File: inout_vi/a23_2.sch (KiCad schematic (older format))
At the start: 27 parts, among them U23029 74HC02, U23030 74HC27, U23031 74HC02, U23032 74HC04, U23034 74HC02, U23035 74HC02, U23036 74HC02, U23037 74HC02, U23038 74HC27, U23039 74HC02, U23040 74HC02, U23041 74HC02, U23042 74HC02, U23043 74HC02, U23044 74HC02, U23045 74HC02, U23046 74HC02, U23047 74HC27, U23048 74HC04, U23049 74HC02, U23050 74HC02, U23051 74HC02, U23052 74HC02, U23053 74HC02, U23054 74HC04, U23055 74HC02, U23056 74HC02

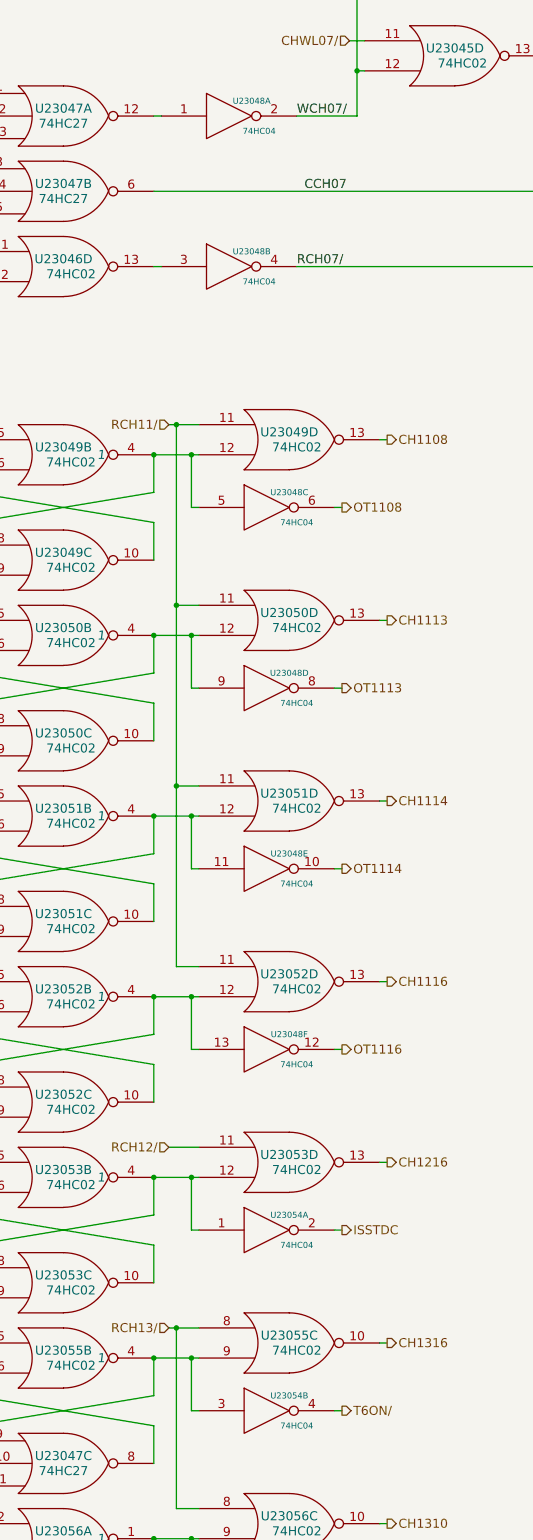
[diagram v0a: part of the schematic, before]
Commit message: Lots of initial conditions, some missed gates, and some wiring fixes
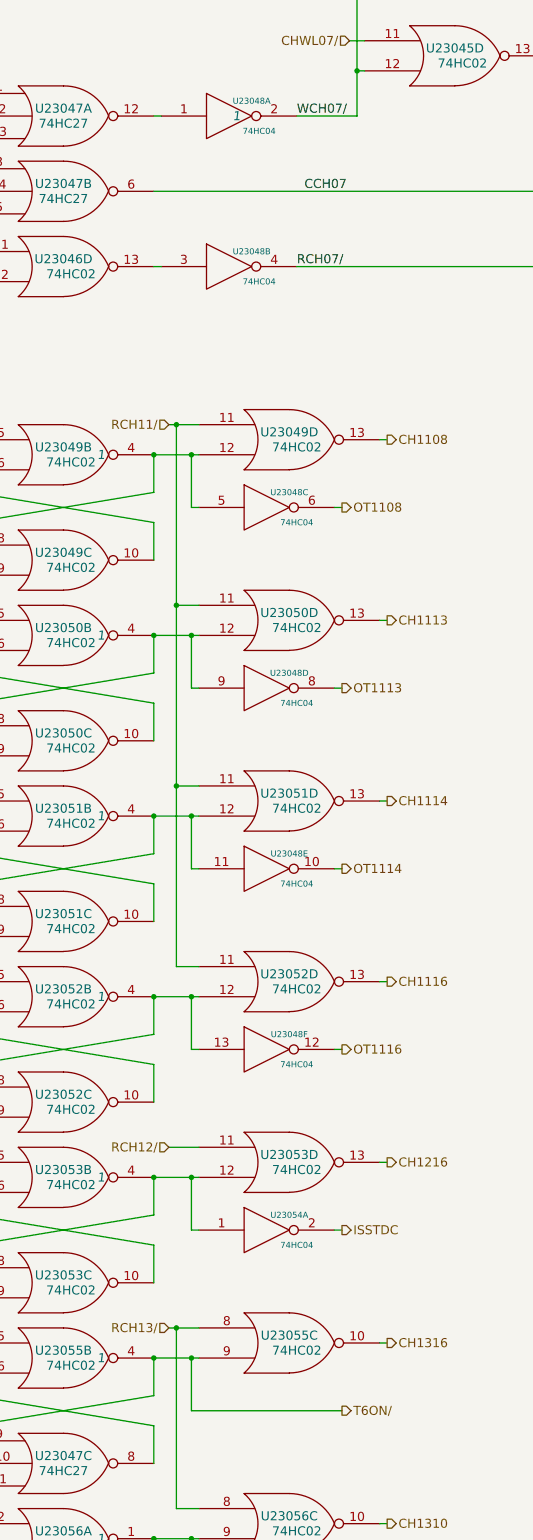
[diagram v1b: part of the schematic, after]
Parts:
- removed unit 2 of U23054
- U23048: Initial (none) -> 1
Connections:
- net T6ON/: now also U23047.9, U23055.4, U23055.9
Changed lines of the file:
@@
 F 2 "" H 13700 3850 60  0000 C CNN
 F 3 "" H 13700 3850 60  0000 C CNN
+F 4 "1" H 13750 3850 60  0000 C CIN "Initial"
 	1    13700 3850
 	1    0    0    -1
@@
 	13450 12100 13450 12450
 Wire Wire Line
-	13450 12450 13500 12450
+	13450 12450 14450 12450
 Connection ~ 13450 12100
-$Comp
-L 74HC04 U23054
-U 2 1 574C5B2F
-P 13950 12450
-F 0 "U23054" H 14100 12550 40  0000 C CNN
-F 1 "74HC04" H 14150 12350 40  0000 C CNN
-F 2 "" H 13950 12450 60  0000 C CNN
-F 3 "" H 13950 12450 60  0000 C CNN
-	2    13950 12450
-	1    0    0    -1
-$EndComp
-Wire Wire Line
-	14400 12450 14450 12450
 Text HLabel 14450 12450 2    60   Output ~ 0
 T6ON/

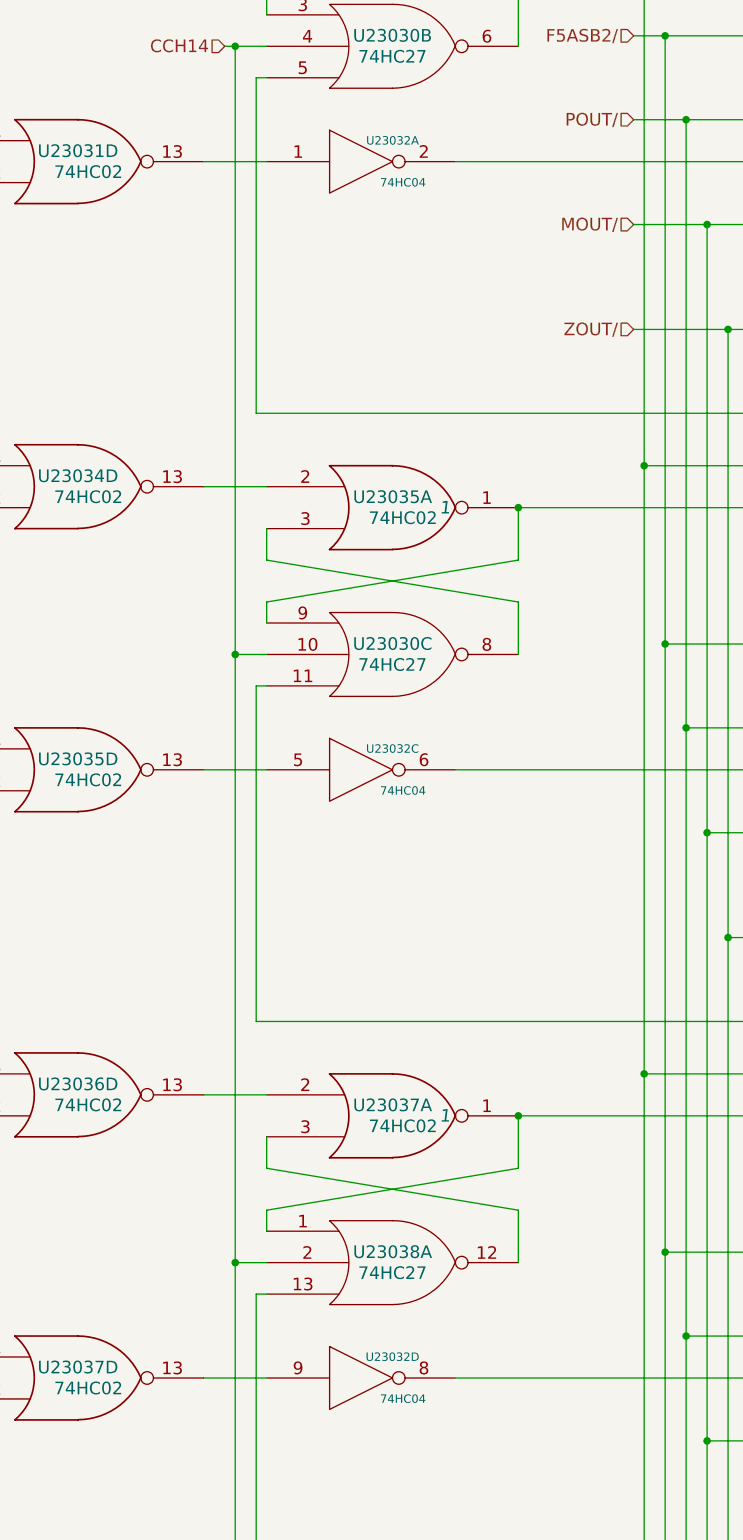
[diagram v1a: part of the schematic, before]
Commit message: Broke out some PIPA and CDU-related output signals, and fixed the polarity of PIPPLS/
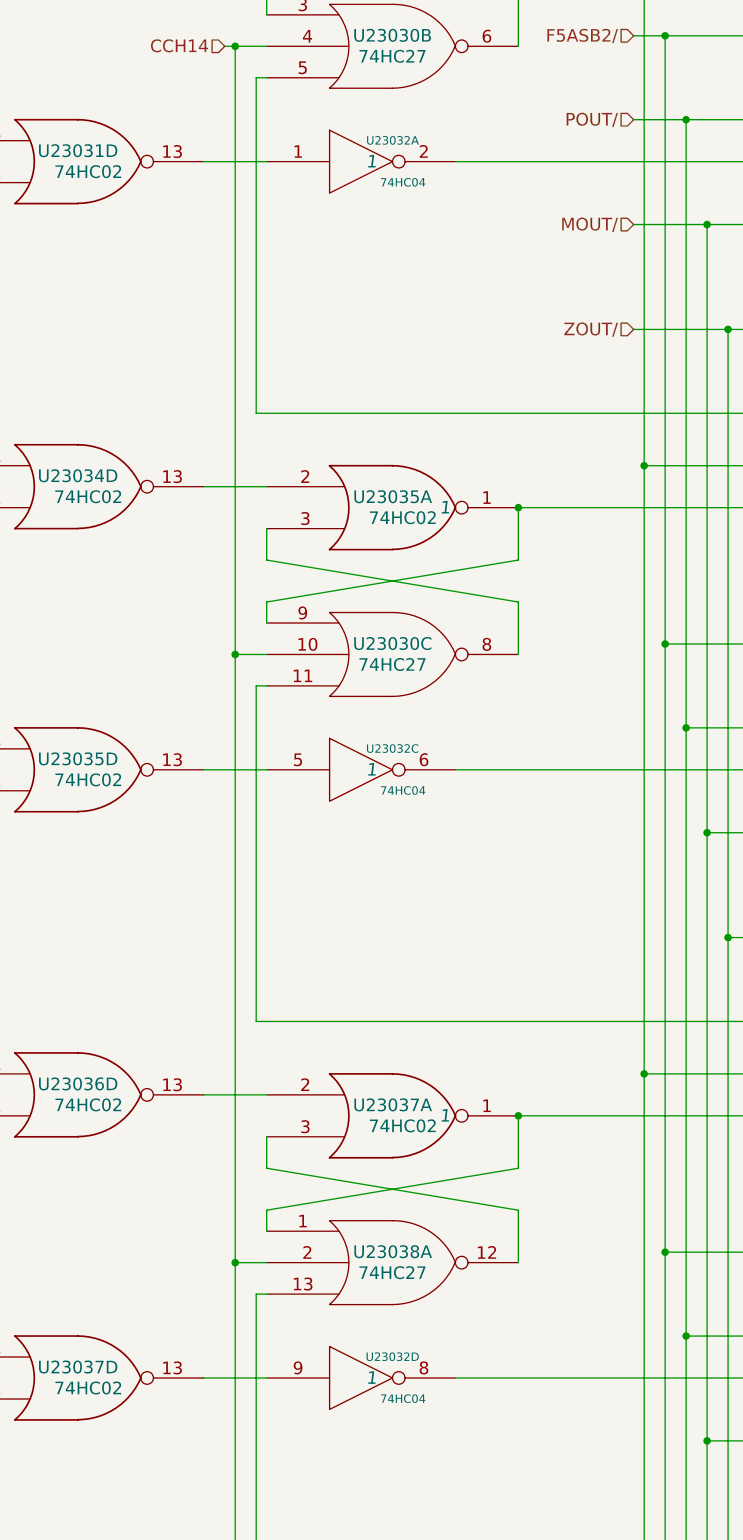
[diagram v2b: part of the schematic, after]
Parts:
- U23032: Initial (none) -> 1
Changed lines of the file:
@@
 F 2 "" H 4050 2350 60  0000 C CNN
 F 3 "" H 4050 2350 60  0000 C CNN
+F 4 "1" H 4100 2350 60  0000 C CIN "Initial"
 	1    4050 2350
 	1    0    0    -1
@@
 F 2 "" H 4050 5250 60  0000 C CNN
 F 3 "" H 4050 5250 60  0000 C CNN
+F 4 "1" H 4100 5250 60  0000 C CIN "Initial"
 	3    4050 5250
 	1    0    0    -1
@@
 F 2 "" H 4050 8150 60  0000 C CNN
 F 3 "" H 4050 8150 60  0000 C CNN
+F 4 "1" H 4100 8150 60  0000 C CIN "Initial"
 	4    4050 8150
 	1    0    0    -1

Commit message: Fixed not->1-input nor in the rest of the modules.
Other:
- moved on the sheet: U23029D, U23030B, U23030C, U23031A, U23031B, U23031C, U23031D, U23032A, U23032B, U23032C, U23032D, U23032E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

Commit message: Updated Inout VI to be on +4VSW
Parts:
- renumbered U23034 to U23033, U23035 to U23034, U23036 to U23035, U23037 to U23036, U23038 to U23037, U23039 to U23038, U23040 to U23039, U23041 to U23040, U23042 to U23041, U23043 to U23042, U23044 to U23043, U23045 to U23044, U23046 to U23045, U23047 to U23046, U23048 to U23047, U23049 to U23048, U23050 to U23049, U23051 to U23050, U23052 to U23051, U23053 to U23052, U23054 to U23053, U23055 to U23054, U23056 to U23055
